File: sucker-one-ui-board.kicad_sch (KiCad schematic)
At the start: 32 parts, among them J1 52271-1079, Q1 BSS138, SW1 LIFT, SW2 LOW, SW3 REVERSE, SW4 TRIGGER, SW5 DROP, SW6 HIGH, U1 WS2812-2020, U10 WS2812-2020, U11 WS2812-2020, U12 WS2812-2020, U2 WS2812-2020, U3 WS2812-2020, U4 WS2812-2020, U5 WS2812-2020, U6 WS2812-2020, U7 WS2812-2020, U8 WS2812-2020, U9 WS2812-2020

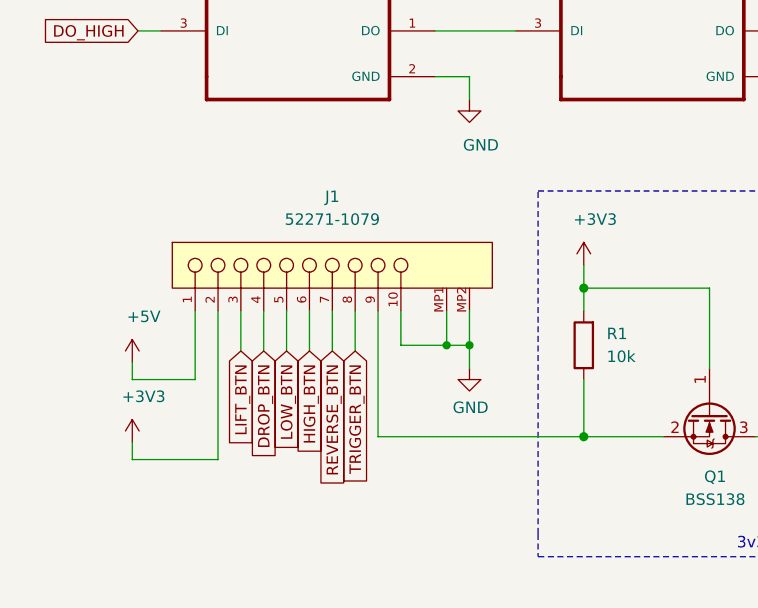
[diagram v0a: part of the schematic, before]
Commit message: Flipped FFC connector and generated gerbers
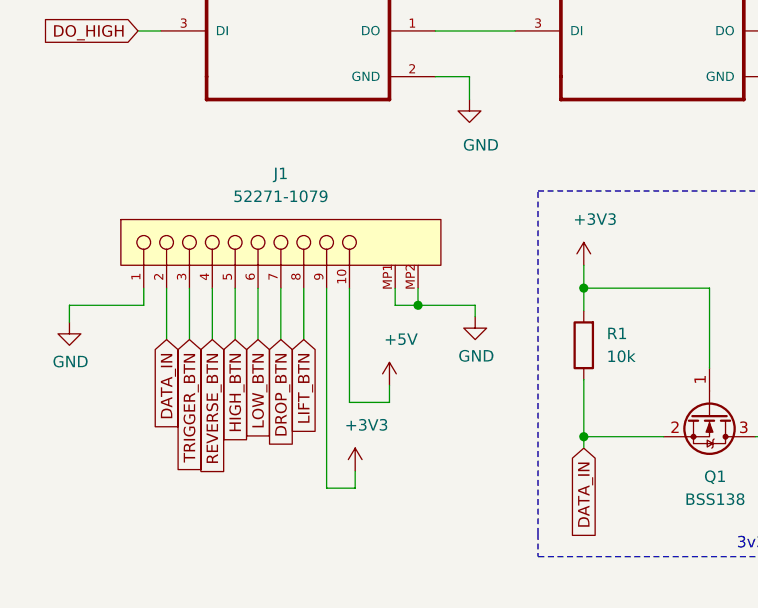
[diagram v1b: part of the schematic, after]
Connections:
- net +3V3: now also J1.9; no longer J1.2
- net +5V: now also J1.10; no longer J1.1
- net DROP_BTN: now also J1.7; no longer J1.4
- net GND: now also J1.1; no longer J1.10
- net HIGH_BTN: now also J1.5; no longer J1.6
- net LIFT_BTN: now also J1.8; no longer J1.3
- net LOW_BTN: now also J1.6; no longer J1.5
- net REVERSE_BTN: now also J1.4; no longer J1.7
- net TRIGGER_BTN: now also J1.3; no longer J1.8
- net DATA_IN: now reaches Q1.2 (S), R1.1
- net DATA_IN: now also J1.2; no longer J1.9

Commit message: Updated and ordered ref 2
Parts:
- added C1, C2, C3, C4, C5, C6: 100n, Capacitor_SMD:C_0603_1608Metric, symbol Device:C
- added C7: 50p, Capacitor_SMD:C_0603_1608Metric, symbol Device:C
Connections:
- net +5V: now also C1.1, C2.1, C3.1, C4.1, C5.1, C6.1
- net DATA_IN: now also C7.1
- net GND: now also C1.2, C2.2, C3.2, C4.2, C5.2, C6.2, C7.2
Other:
- moved on the sheet: J1, Q1, R1, R2, SW4, U12, U9

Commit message: Refactorings
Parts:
- removed J1: 52271-1079, Molex-52271-1079-*:Molex-52271-1079-Manufacturer_Recommended, symbol MOLEX 10 Pin 1mm FFC con:52271-1079
- removed Q1: BSS138, Package_TO_SOT_SMD:SOT-23, symbol Transistor_FET:BSS138
- removed R1, R2: 10k, Resistor_SMD:R_0603_1608Metric, symbol Device:R
- added J1: BM10B-SRSS-TB(LF)(SN), BM10B-SRSS-TB(LF)(SN):BM10B-SRSS-TB(LF)(SN), symbol BM10B-SRSS-TB(LF)(SN):BM10B-SRSS-TB(LF)(SN)
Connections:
- net DATA_IN is gone; now on net LED_DATA: C7.1
- net +3V3: now also J1.9
- net +5V: now also J1.10
- net DROP_BTN: now also J1.7
- net GND: now also J1.1, J1.S1 (SHIELD), J1.S2 (SHIELD)
- net HIGH_BTN: now also J1.5
- net LED_DATA: now also J1.2
- net LIFT_BTN: now also J1.8
- net LOW_BTN: now also J1.6
- net REVERSE_BTN: now also J1.4
- net TRIGGER_BTN: now also J1.3
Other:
- note removed: "3v3 <> 5v Logic Level Shift"
- moved on the sheet: C7

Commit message: Cleanup and generate iBOM
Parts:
- TP1, TP10, TP2, TP3, TP4, TP5, TP6, TP7, TP8, TP9: now left out of the parts list
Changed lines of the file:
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@@
   )
   (symbol (lib_id "Connector:TestPoint") (at 128.905 162.56 0) (unit 1)
-    (in_bom yes) (on_board yes)
+    (in_bom no) (on_board yes)
     (property "Reference" "TP2" (id 0) (at 131.445 160.02 0)
       (effects (font (size 1.27 1.27)) (justify left))
@@
   )
   (symbol (lib_id "Connector:TestPoint") (at 128.905 180.34 0) (unit 1)
-    (in_bom yes) (on_board yes)
+    (in_bom no) (on_board yes)
     (property "Reference" "TP3" (id 0) (at 131.445 177.8 0)
       (effects (font (size 1.27 1.27)) (justify left))
@@
   )
   (symbol (lib_id "Connector:TestPoint") (at 139.065 162.56 0) (unit 1)
-    (in_bom yes) (on_board yes)
+    (in_bom no) (on_board yes)
     (property "Reference" "TP4" (id 0) (at 141.605 160.02 0)
       (effects (font (size 1.27 1.27)) (justify left))
@@
   )
   (symbol (lib_id "Connector:TestPoint") (at 139.065 180.34 0) (unit 1)
-    (in_bom yes) (on_board yes)
+    (in_bom no) (on_board yes)
     (property "Reference" "TP5" (id 0) (at 141.605 177.8 0)
       (effects (font (size 1.27 1.27)) (justify left))
@@
   )
   (symbol (lib_id "Connector:TestPoint") (at 152.4 162.56 0) (unit 1)
-    (in_bom yes) (on_board yes)
+    (in_bom no) (on_board yes)
     (property "Reference" "TP6" (id 0) (at 154.94 160.02 0)
       (effects (font (size 1.27 1.27)) (justify left))
@@
   )
   (symbol (lib_id "Connector:TestPoint") (at 152.4 180.34 0) (unit 1)
-    (in_bom yes) (on_board yes)
+    (in_bom no) (on_board yes)
     (property "Reference" "TP7" (id 0) (at 154.94 177.8 0)
       (effects (font (size 1.27 1.27)) (justify left))
@@
   )
   (symbol (lib_id "Connector:TestPoint") (at 166.37 162.56 0) (unit 1)
-    (in_bom yes) (on_board yes)
+    (in_bom no) (on_board yes)
     (property "Reference" "TP8" (id 0) (at 168.91 160.02 0)
       (effects (font (size 1.27 1.27)) (justify left))
@@
   )
   (symbol (lib_id "Connector:TestPoint") (at 166.37 180.34 0) (unit 1)
-    (in_bom yes) (on_board yes)
+    (in_bom no) (on_board yes)
     (property "Reference" "TP9" (id 0) (at 168.91 177.8 0)
       (effects (font (size 1.27 1.27)) (justify left))
@@
   )
   (symbol (lib_id "Connector:TestPoint") (at 258.445 149.225 0) (unit 1)
-    (in_bom yes) (on_board yes)
+    (in_bom no) (on_board yes)
     (property "Reference" "TP1" (id 0) (at 260.985 146.685 0)
       (effects (font (size 1.27 1.27)) (justify left))
@@
   )
   (symbol (lib_id "Connector:TestPoint") (at 265.43 125.095 0) (unit 1)
-    (in_bom yes) (on_board yes)
+    (in_bom no) (on_board yes)
     (property "Reference" "TP10" (id 0) (at 267.97 122.555 0)
       (effects (font (size 1.27 1.27)) (justify left))
